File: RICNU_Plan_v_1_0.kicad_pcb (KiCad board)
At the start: 4 copper layers, 50 x 55 mm, 232 parts, among them J1 USB_OTG, J2 MOLEX-PC6, J3 DF52-4S-0.8H(21), J4 DF52-4S-0.8H(21), J5 MOLEX-PC20, J6 2x0.1, J7 FH19C-6S-0.5SH(05), Q1 N-CH, Q2 N-CH, SW1 CL-SB-12B-01T, SW2 SW_Push_4pin, SW3 SW_Push_4pin, U1 TPS2113, U2 TLV62568, U3 SN74AHC126, U4 FT232RL, U5 TCAN334G, U6 SN65HVD75, U7 BT121, U8 STM32F103RC, Y1 Crystal

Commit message: Design freeze - ordered the board
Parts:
- added G***: LOGO, RICNU_Plan_v_1_0:SRALAB-3.5mm, F.Cu at (124.8, 88.5)
- added G***: LOGO, RICNU_Plan_v_1_0:AR122017-1.50mm, F.Cu at (144.0, 120.2)
- added G***: LOGO, RICNU_Plan_v_1_0:CBM-2mm, F.Cu at (124.8, 127.0)
- added G***: LOGO, RICNU_Plan_v_1_0:RICNUPlan_1-0_3.5mm, F.Cu at (139.5, 115.2)
- added R96: 470, Resistors_SMD:R_0402_NoSilk, F.Cu at (152.8, 101.2)
- added R97: 10k, Resistors_SMD:R_0402_NoSilk, F.Cu at (152.8, 100.2)
- added R98: 10k, Resistors_SMD:R_0402_NoSilk, B.Cu at (155.4, 108.3)
- added R99: 470, Resistors_SMD:R_0402_NoSilk, B.Cu at (155.4, 110.8)
- added REF***: OSHW-Logo_5.7x6mm_SilkScreen, Symbols:OSHW-Logo_5.7x6mm_SilkScreen, F.Cu at (148.9, 109.6)
- added REF***: KiCad-Logo2_6mm_SilkScreen, Symbols:KiCad-Logo2_6mm_SilkScreen, B.Cu at (129.3, 105.7)
- C15: moved to F.Cu
- D6: value LED -> LED_R
- D7: value LED -> LED_Y
- D8: value LED -> LED_G
- D9: value LED -> LED_B
- R78: value R -> 660; moved to B.Cu
- R79: value R -> 470; moved to B.Cu
- R80: value R -> 330; moved to B.Cu
- R81: value R -> 180; moved to B.Cu
- moved C15 27.9 mm to (167.9, 105.5), turned to 0 degrees
- moved SW3 27.4 mm to (167.9, 102.3), turned to 90 degrees
- moved R81 14.7 mm to (154.2, 94.3), turned to 270 degrees
- moved R80 14.3 mm to (155.2, 94.3), turned to 270 degrees
- moved R79 14.1 mm to (156.2, 94.3), turned to 270 degrees
- moved R78 14.0 mm to (157.2, 94.3), turned to 270 degrees
- moved D9 11.3 mm to (154.6, 99.3), turned to 90 degrees
- moved D8 10.2 mm to (155.8, 99.3), turned to 90 degrees
- moved D7 9.34 mm to (157.0, 99.3), turned to 90 degrees
- moved D6 8.68 mm to (158.2, 99.3), turned to 90 degrees
- moved C7 0.80 mm to (147.1, 98.7)
- moved C8 0.80 mm to (149.2, 98.7)
- moved R12 0.80 mm to (148.5, 93.7)
- moved U4 0.80 mm to (149.9, 93.4)
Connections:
- D15 pad 2: /BT_UART_TX -> /BT_BOOT0
- R10 pad 1: /BT_UART_TX -> /BT_BOOT0
- R20 pad 2: /Bluetooth/BT.RX -> /BT_UART_RX
- R9 pad 2: /Bluetooth/BT.RX -> /BT_UART_RX
- SW1 pad 1: /BT_UART_TX -> /BT_BOOT0
- U3 pad 10: /BT_UART_TX -> /BT_BOOT0
- U3 pad 12: /BT_UART_RX -> /BT_UART_TX
- U3 pad 13: /BT_UART_TX -> /BT_BOOT0
- U3 pad 2: /BT_UART_RX -> /BT_UART_TX
- U3 pad 6: /Bluetooth/BT.RX -> /BT_UART_RX
- U7 pad 23: /BT_UART_TX -> /BT_BOOT0
- U7 pad 28: /Bluetooth/BT.RX -> /BT_UART_RX
- U7 pad 29: /BT_UART_RX -> /BT_UART_TX
- U8 pad 15: /LED1 -> /LED4
- U8 pad 25: Net-(U8-Pad25) -> /LED1
- U8 pad 28: /LED4 -> /MCU/MCU_BOOT1
- U8 pad 60: Net-(U8-Pad60) -> /MCU/MCU_BOOT0
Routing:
- net /BT_BOOT0: track 0.00 -> 30.2 mm, vias 0 -> 3
- net /Bluetooth/BT.RX: track 24.6 -> 0.00 mm, vias 1 -> 0
- net /MCU/MCU_SWD_RESET: track 12.9 -> 24.3 mm, vias 1 -> 3
- net /BT_UART_TX: track 30.2 -> 19.6 mm, vias 3 -> 2
- net /MCU/MCU_BOOT0: track 0.00 -> 10.5 mm, vias 0 -> 1
- net /MCU/MCU_BOOT1: track 0.00 -> 7.66 mm
- net /LED3: track 11.2 -> 5.62 mm, vias 2 -> 0
- net /BT_UART_RX: track 19.6 -> 24.6 mm, vias 2 -> 1
- net /LED4: track 12.6 -> 17.5 mm
- net /LED2: track 10.2 -> 5.33 mm, vias 2 -> 0
- net GND: track 158.8 -> 162.8 mm, vias 62 -> 65
- net /MCU/MCU_VCC: track 84.0 -> 80.1 mm
- net /LED/LED4_R: track 1.00 -> 4.66 mm, vias 0 -> 1
- net /LED/LED3_R: track 1.00 -> 4.41 mm, vias 0 -> 1
- net /LED/LED1_R: track 1.00 -> 4.41 mm, vias 0 -> 1
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- added copper zone on B.Cu, net /MCU/MCU_VCC
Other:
- rule pad_to_mask_clearance: 0.15 -> 0
- board text added: "MCU RST"
- board text added: "SPI"
- board text added: "SWD"
- board text removed: "Alexey Revinski"
- board text removed: "DEBUG"
- board text removed: "MCU RESET"
- board text removed: "RICNU Plan 0.1"
- board text removed: "Shirley Ryan"
- board text removed: "bility"
- board text removed: "lab"
- board text removed: "y"

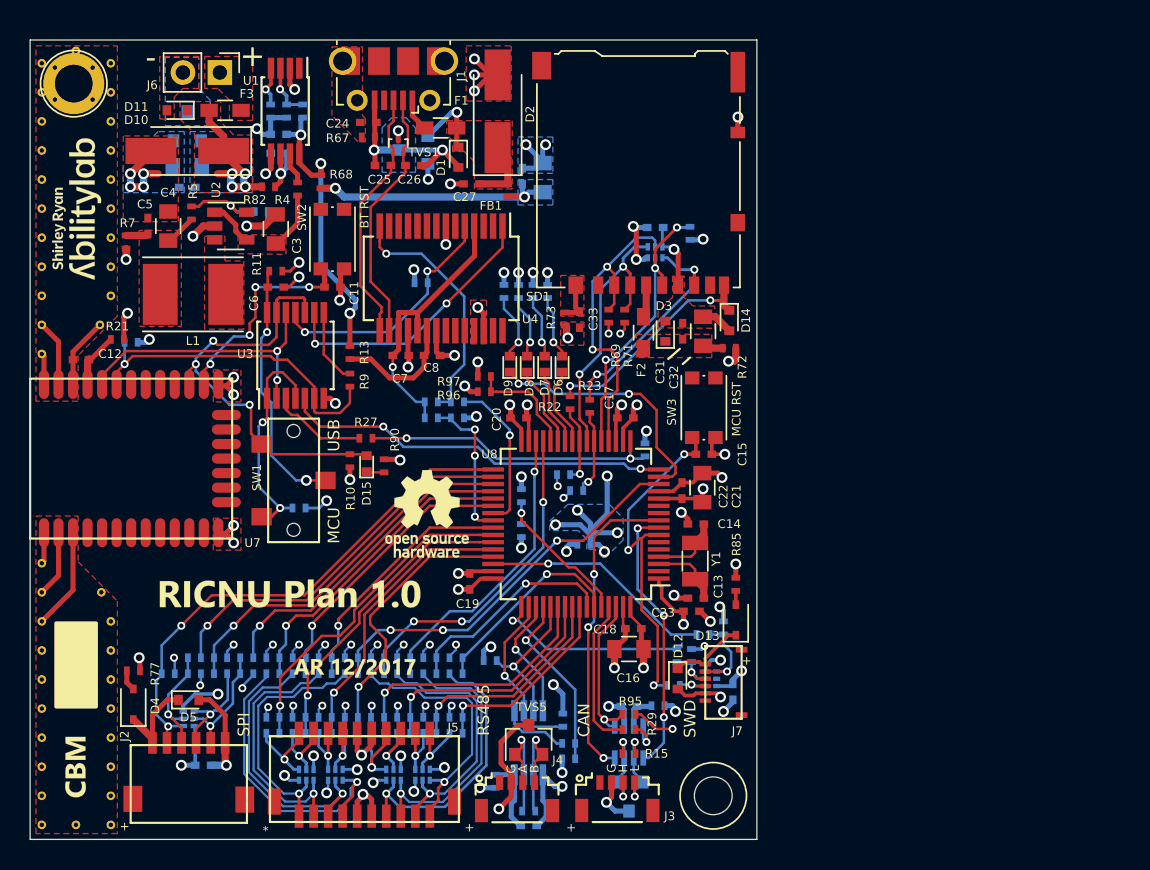
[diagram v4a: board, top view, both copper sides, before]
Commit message: Various small changes like comment removal
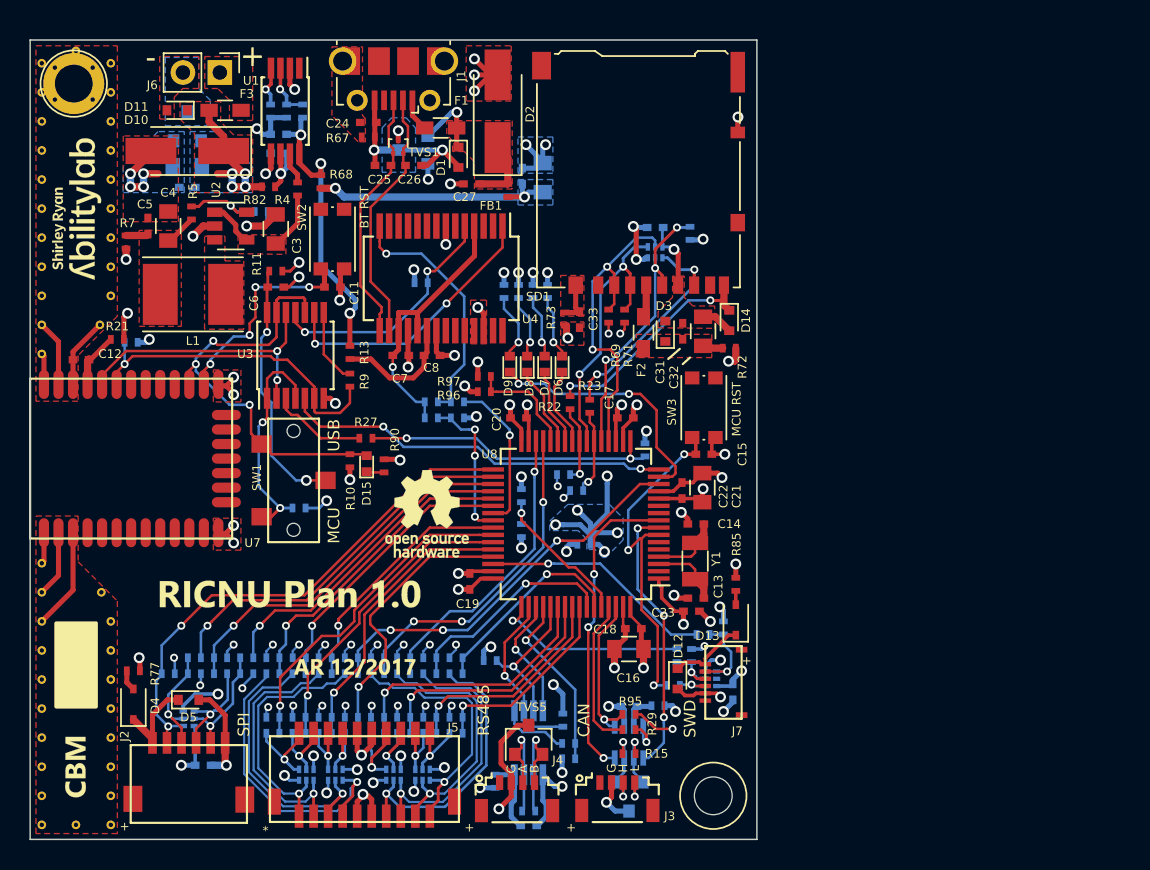
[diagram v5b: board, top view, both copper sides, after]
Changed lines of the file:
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@@
     (links 487)
     (no_connects 7)
-    (area 121.594999 76.994999 171.605001 132.005001)
+    (area 121.549999 76.949999 171.650001 132.050001)
     (thickness 1.6)
     (drawings 50)
@@
   (layers
     (0 F.Cu signal)
-    (1 In1.Cu power hide)
+    (1 In1.Cu power)
     (2 In2.Cu power hide)
     (31 B.Cu signal)
-    (34 B.Paste user)
+    (34 B.Paste user hide)
     (35 F.Paste user)
     (36 B.SilkS user)
-    (37 F.SilkS user)
-    (38 B.Mask user)
+    (37 F.SilkS user hide)
+    (38 B.Mask user hide)
     (39 F.Mask user)
     (44 Edge.Cuts user)
@@
     (solder_mask_min_width 0.1016)
     (aux_axis_origin 121.6 132)
-    (visible_elements 7FFEF67F)
+    (visible_elements 7FFEFE7F)
     (pcbplotparams
-      (layerselection 0x00030_80000001)
+      (layerselection 0x0100c_00000000)
       (usegerberextensions false)
       (excludeedgelayer true)
@@
       (psnegative false)
       (psa4output false)
-      (plotreference true)
-      (plotvalue true)
+      (plotreference false)
+      (plotvalue false)
       (plotinvisibletext false)
       (padsonsilk false)
@@
       (drillshape 0)
       (scaleselection 1)
-      (outputdirectory ""))
+      (outputdirectory ./))
   )
   (net 0 "")
@@
     (arrow2b (pts (xy 121.6 70.75) (xy 122.726504 70.163579)))
   )
-  (gr_line (start 171.6 77) (end 121.6 77) (layer Edge.Cuts) (width 0.01))
-  (gr_line (start 171.6 132) (end 171.6 77) (layer Edge.Cuts) (width 0.01))
-  (gr_line (start 121.6 132) (end 171.6 132) (layer Edge.Cuts) (width 0.01))
-  (gr_line (start 121.6 77) (end 121.6 132) (layer Edge.Cuts) (width 0.01))
+  (gr_line (start 171.6 77) (end 121.6 77) (layer Edge.Cuts) (width 0.1))
+  (gr_line (start 171.6 132) (end 171.6 77) (layer Edge.Cuts) (width 0.1))
+  (gr_line (start 121.6 132) (end 171.6 132) (layer Edge.Cuts) (width 0.1))
+  (gr_line (start 121.6 77) (end 121.6 132) (layer Edge.Cuts) (width 0.1))
   (segment (start 141.6 86.030322) (end 141.6 85.499992) (width 0.35) (layer B.Cu) (net 1))
   (segment (start 141.6 92.489998) (end 141.6 86.030322) (width 0.35) (layer B.Cu) (net 1))
@@
   (segment (start 136.4 87.1) (end 137.55 87.1) (width 0.5) (layer F.Cu) (net 25) (status 20))
   (segment (start 135.4 86.2) (end 134.5 86.2) (width 0.5) (layer F.Cu) (net 25))
-  (segment (start 135.4 87.1) (end 135.4 86.2) (width 0.5) (layer B.Cu) (net 25))
+  (segment (start 135.5 87.1) (end 135.5 86.2) (width 0.5) (layer B.Cu) (net 25))
   (via (at 135.5 86.2) (size 0.75) (drill 0.45) (layers F.Cu B.Cu) (net 25))
   (segment (start 136.3 87.1) (end 135.4 87.1) (width 0.5) (layer F.Cu) (net 25))
   (via (at 135.5 87.1) (size 0.75) (drill 0.45) (layers F.Cu B.Cu) (net 25))
-  (segment (start 136.3 86.2) (end 136.3 87.1) (width 0.5) (layer B.Cu) (net 25))
+  (segment (start 136.4 86.2) (end 136.4 87.1) (width 0.5) (layer B.Cu) (net 25))
   (via (at 136.4 87.1) (size 0.75) (drill 0.45) (layers F.Cu B.Cu) (net 25))
   (segment (start 134.911446 84.636814) (end 134.911446 84.811446) (width 0.5) (layer F.Cu) (net 25) (status 30))
@@
     (min_thickness 0.254)
     (keepout (tracks not_allowed) (vias allowed) (copperpour not_allowed))
-    (fill yes (arc_segments 16) (thermal_gap 0.508) (thermal_bridge_width 0.508))
+    (fill (arc_segments 16) (thermal_gap 0.508) (thermal_bridge_width 0.508))
     (polygon
       (pts
